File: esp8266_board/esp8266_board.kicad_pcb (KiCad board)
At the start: 2 copper layers, 50 x 25 mm, 8 parts, among them J1 Screw_Terminal_01x04, J2 Conn_01x08_Pin, J3 Screw_Terminal_01x02, SW1 SW_Push, SW2 SW_Push

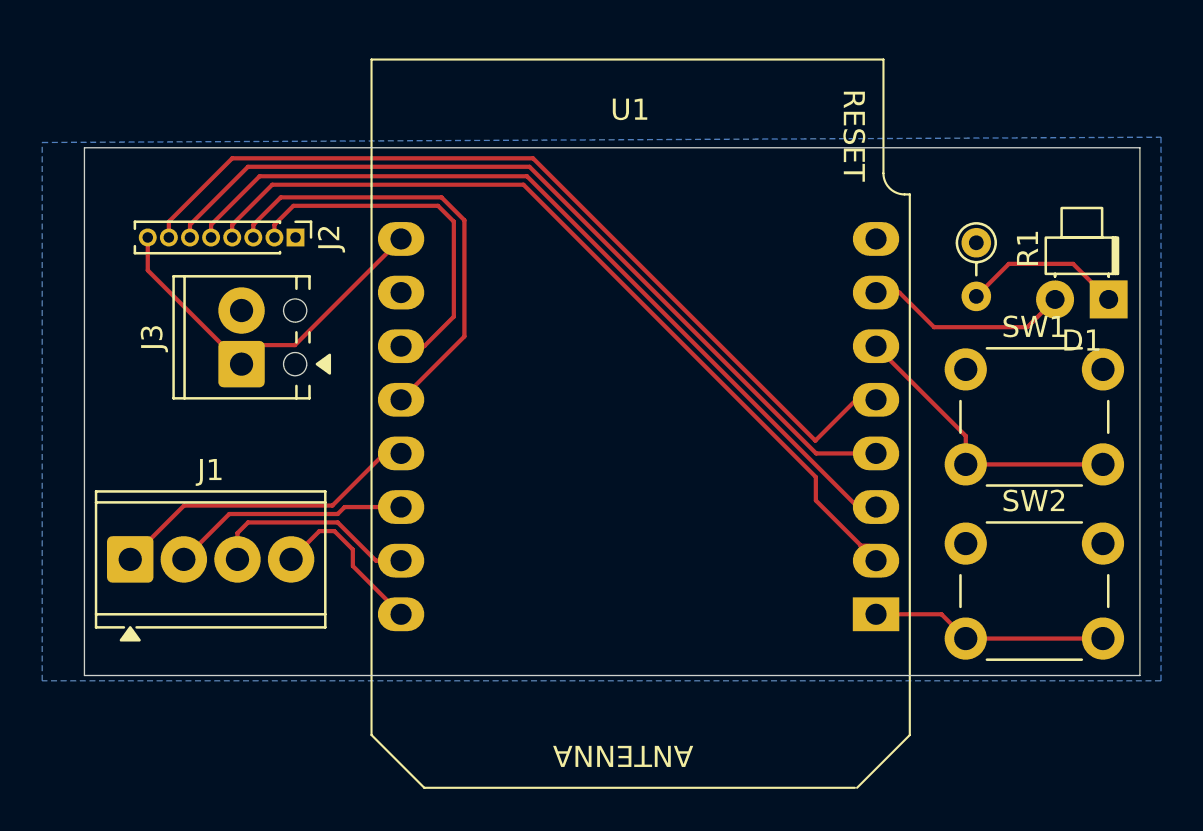
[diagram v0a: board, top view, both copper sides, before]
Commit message: Add mounting holes, silkscreen edits, final layout
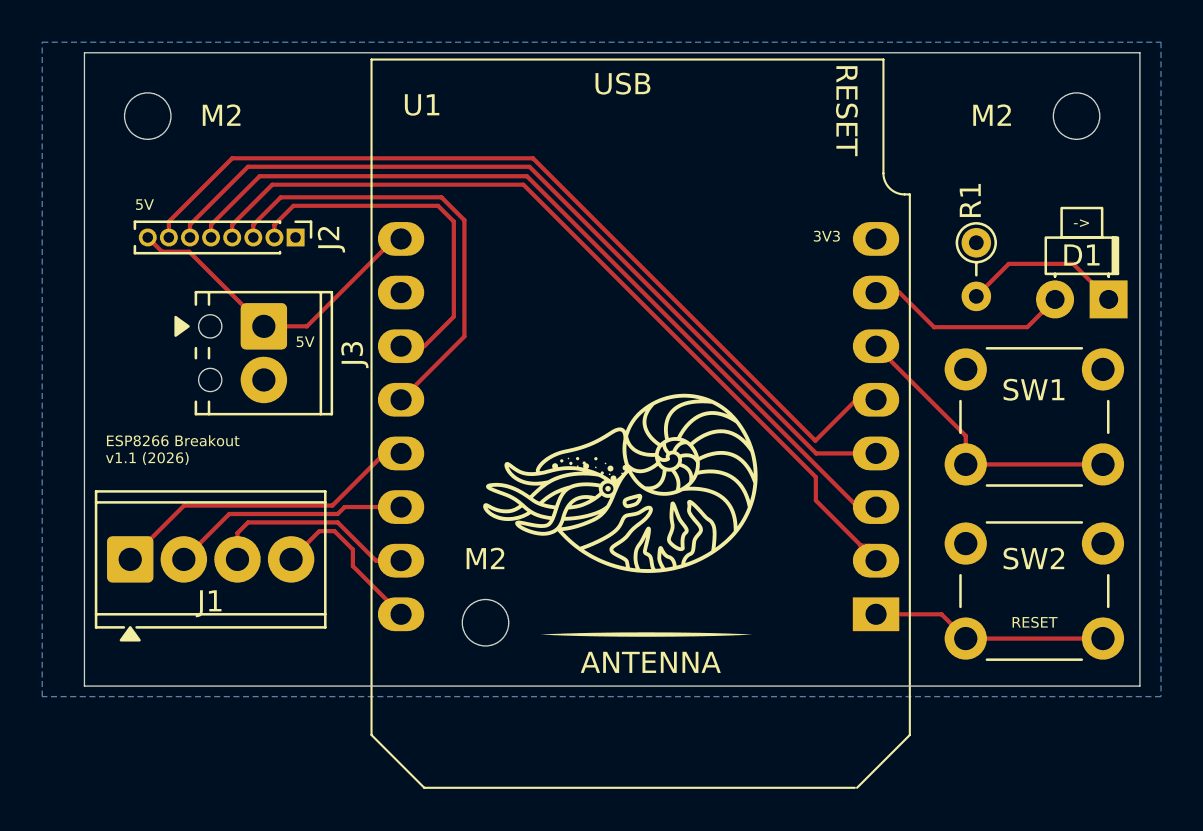
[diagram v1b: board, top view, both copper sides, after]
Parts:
- added M2: MountingHole_2.2mm_M2, MountingHole:MountingHole_2.2mm_M2, F.Cu at (161.0, 71.0)
- added M2: MountingHole_2.2mm_M2, MountingHole:MountingHole_2.2mm_M2, F.Cu at (145.0, 47.0)
- added M2: MountingHole_2.2mm_M2, MountingHole:MountingHole_2.2mm_M2, F.Cu at (189.0, 47.0)
- moved J3 2.08 mm to (150.5, 57.0), turned to -90 degrees
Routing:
- net Net-(J2-Pin_8): track 17.9 -> 16.3 mm
- added copper zone on B.Cu, net GND
- removed copper zone on B.Cu, net (none)
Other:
- board size 50 x 25 mm -> 50 x 30 mm
- board text added: "->"
- board text added: "3V3"
- board text added: "5V"
- board text added: "ESP8266 Breakout v1.1 (2026)"
- board text added: "RESET"
- board text added: "USB"
